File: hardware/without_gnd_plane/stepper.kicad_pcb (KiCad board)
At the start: 4 copper layers, 40 x 40 mm, 132 parts, among them J101 USB-MINI-B-SMD, J102 DRILL, J103 DRILL, J104 DRILL, J105 DRILL, J401 STACK-UP-HIGH, J402 STACK-DOWN, J403 STACK-UP-HIGH, J404 STACK-DOWN, P201 black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

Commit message: version before changing to 6 layers
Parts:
- removed R201: 0, kicad-libraries:0603E
- C105, C106: value 8pF -> 5pF
- RP201: value 100 -> 220
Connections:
- C101 pad 2: GND -> STACK-PGND
- C102 pad 2: GND -> STACK-PGND
- C103 pad 2: GND -> STACK-PGND
- C104 pad 2: GND -> STACK-PGND
- C105 pad 2: GND -> STACK-PGND
- C106 pad 2: GND -> STACK-PGND
- C301 pad 2: GND -> STACK-PGND
- C302 pad 2: GND -> STACK-PGND
- C303 pad 2: GND -> STACK-PGND
- C304 pad 2: GND -> STACK-PGND
- C401 pad 2: GND -> STACK-PGND
- C402 pad 2: GND -> STACK-PGND
- C403 pad 2: GND -> STACK-PGND
- C404 pad 2: GND -> STACK-PGND
- C501 pad 2: GND -> STACK-PGND
- C502 pad 2: GND -> STACK-PGND
- C503 pad 2: GND -> STACK-PGND
- C504 pad 2: GND -> STACK-PGND
- C505 pad 2: GND -> STACK-PGND
- C506 pad 2: GND -> STACK-PGND
- C507 pad 2: GND -> STACK-PGND
- C508 pad 2: GND -> STACK-PGND
- C509 pad 2: GND -> STACK-PGND
- C510 pad 2: GND -> STACK-PGND
- C511 pad 2: GND -> STACK-PGND
- C512 pad 2: GND -> STACK-PGND
- C513 pad 2: GND -> STACK-PGND
- C514 pad 2: GND -> STACK-PGND
- C515 pad 2: GND -> STACK-PGND
- C516 pad 2: GND -> STACK-PGND
- C517 pad 2: GND -> STACK-PGND
- C518 pad 2: GND -> STACK-PGND
- D301 pad 1: GND -> STACK-PGND
- D302 pad 1: GND -> STACK-PGND
- D401 pad 1: GND -> STACK-PGND
- D402 pad 1: GND -> STACK-PGND
- D502 pad 1: GND -> STACK-PGND
- D503 pad 1: GND -> STACK-PGND
- FB102 pad 1: GND -> STACK-PGND
- FILTER301 pad EXP: GND -> STACK-PGND
- FILTER302 pad 14: GND -> STACK-PGND
- FILTER302 pad EXP: GND -> STACK-PGND
- J101 pad 5: GND -> STACK-PGND
- J401 pad EP: GND -> STACK-PGND
- J402 pad EP: GND -> STACK-PGND
- J403 pad 21: GND -> STACK-PGND
- J403 pad 23: GND -> STACK-PGND
- J403 pad 25: GND -> STACK-PGND
- J403 pad 27: GND -> STACK-PGND
- J403 pad EP: GND -> STACK-PGND
- J404 pad 21: GND -> STACK-PGND
- J404 pad 23: GND -> STACK-PGND
- J404 pad 25: GND -> STACK-PGND
- J404 pad 27: GND -> STACK-PGND
- J404 pad EP: GND -> STACK-PGND
- P301 pad 2: GND -> STACK-PGND
- P301 pad EP: GND -> STACK-PGND
- P302 pad 2: GND -> STACK-PGND
- P302 pad EP: GND -> STACK-PGND
- R104 pad 1: GND -> STACK-PGND
- R203 pad 2: GND -> STACK-PGND
- R207 pad 2: GND -> STACK-PGND
- R208 pad 1: GND -> STACK-PGND
- SW101 pad 2: GND -> STACK-PGND
- U101 pad 17: GND -> STACK-PGND
- U101 pad 2: GND -> STACK-PGND
- U101 pad 46: GND -> STACK-PGND
- U101 pad 60: GND -> STACK-PGND
- U102 pad 2: GND -> STACK-PGND
- U501 pad 1: GND -> STACK-PGND
- X101 pad 3: GND -> STACK-PGND
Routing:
- net GND: track 429.1 -> 0.00 mm, vias 65 -> 0
- net STACK-PGND: track 278.6 -> 692.9 mm, vias 70 -> 135
- removed copper zone on B.Cu, net GND
- removed copper zone on GND, net GND
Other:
- board text added: "Silent Stepper 1.0b"
- board text removed: "Silent Stepper 1.0"

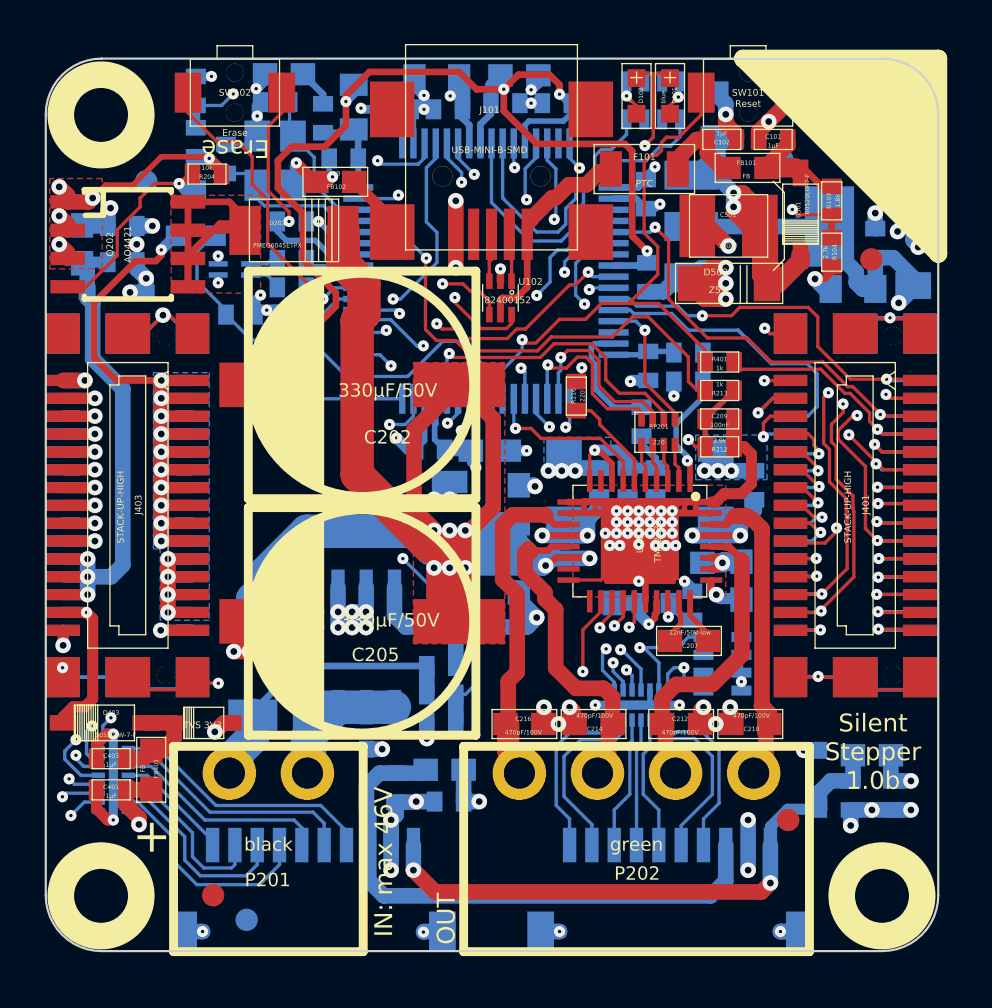
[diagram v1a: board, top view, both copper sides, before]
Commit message: change to 6 layer layout
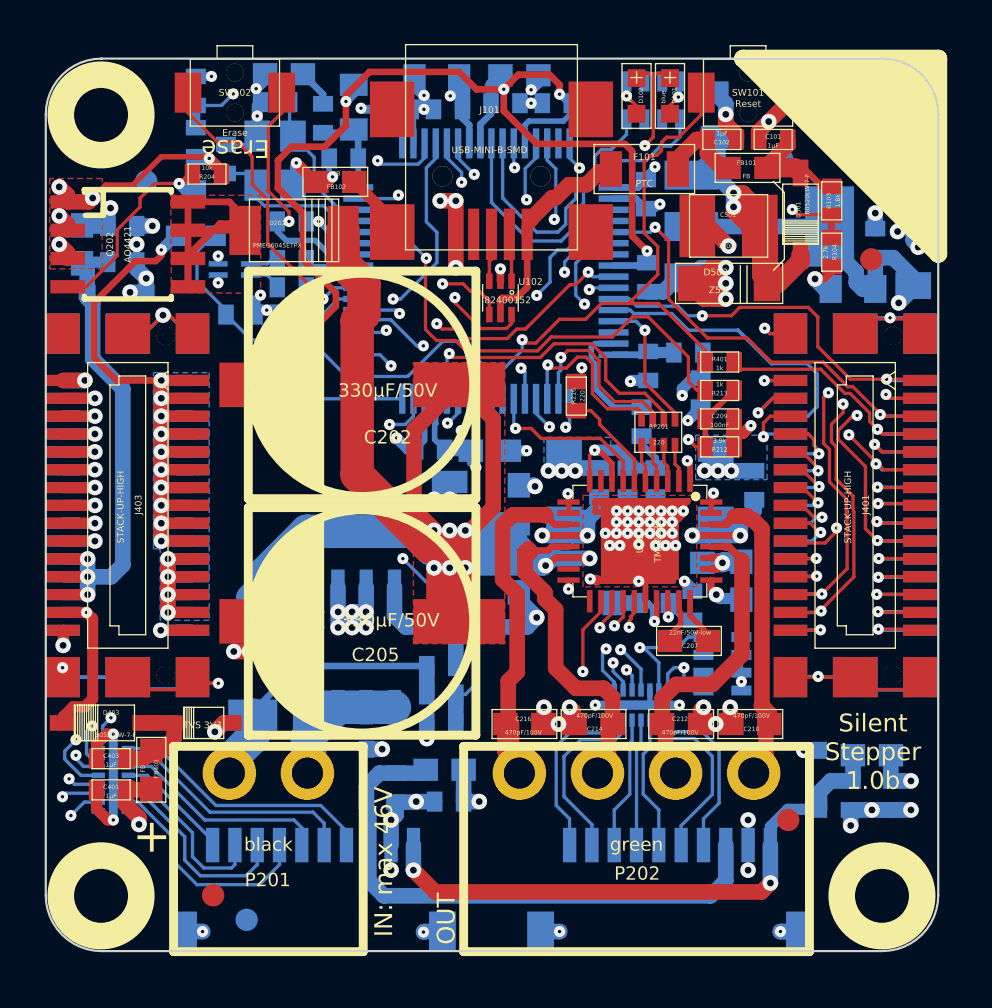
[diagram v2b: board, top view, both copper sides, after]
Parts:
- moved C106 0.74 mm to (156.1, 87.8), turned to 270 degrees
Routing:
- net STACK-PGND: track 692.9 -> 666.4 mm, vias 135 -> 142
- net BRICKLET-IO1_0/AD1: track 47.9 -> 35.4 mm
- net 3V3: track 182.3 -> 176.9 mm
- net BRICKLET-I2C-SCL: track 56.0 -> 58.8 mm
- net Net-(C105-Pad1): track 3.07 -> 4.24 mm
- net STACK-I2C-SCL/JTAG-TDO: track 23.5 -> 24.3 mm
- net STACK-I2C-SDA/JTAG-TDI: track 13.5 -> 14.2 mm
- net STACK-SER-TXD: track 35.8 -> 36.5 mm
- net STACK-SPI-MOSI: track 22.4 -> 23.1 mm
- net STACK-SER-RXD: track 34.7 -> 35.3 mm
- net PWR-CLK: track 6.71 -> 7.00 mm, vias 1 -> 2
- added copper zone on IN4.CU, net STACK-PVCC
- removed copper zone on VCC, net STACK-PVCC
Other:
- copper layers 4 -> 6

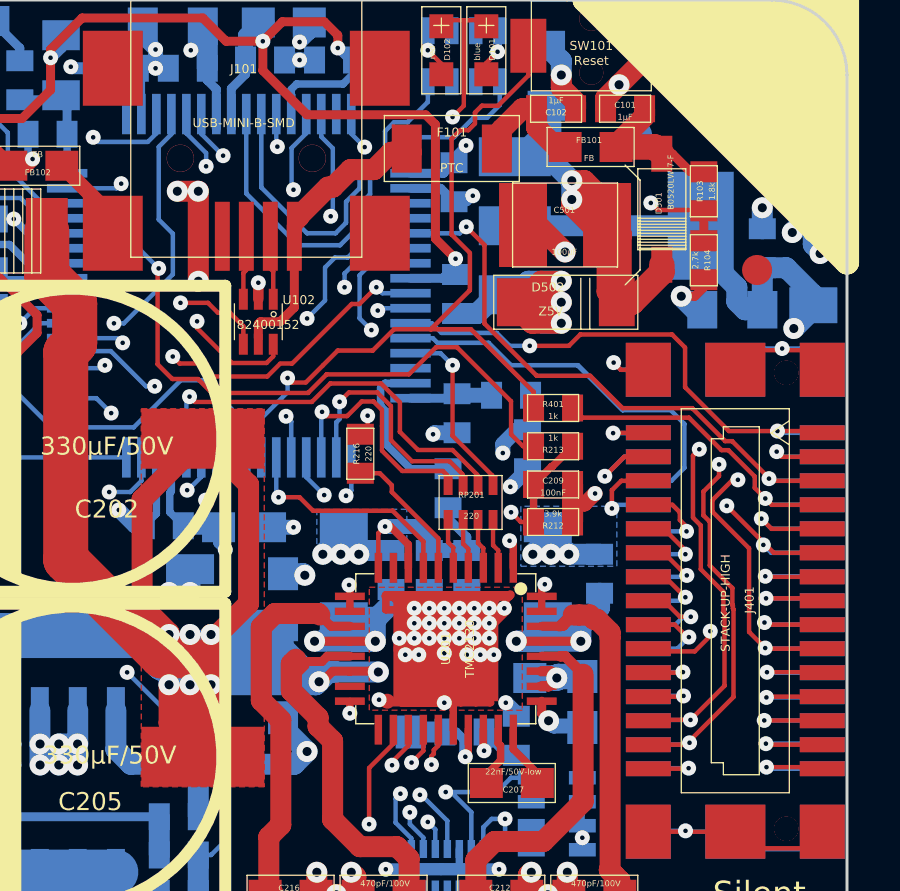
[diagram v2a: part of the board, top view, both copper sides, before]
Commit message: change routing, remove pi filter
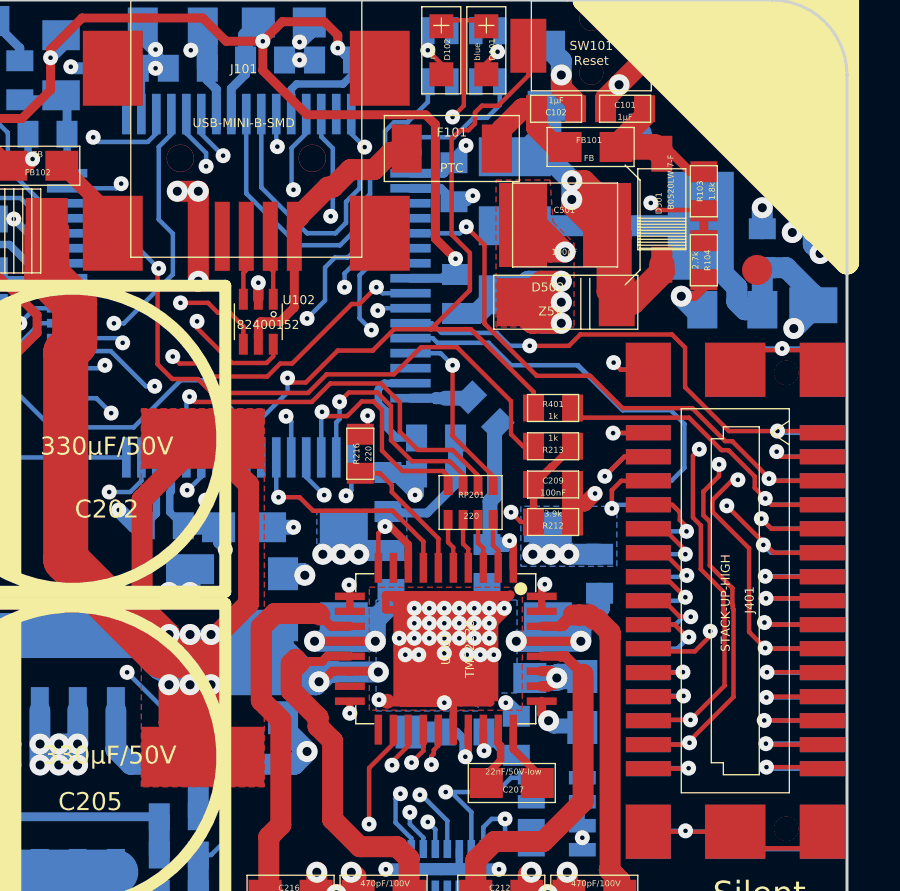
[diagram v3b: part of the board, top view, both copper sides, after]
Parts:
- removed C105, C106: 5pF, kicad-libraries:0402E
- added R201: 1k, kicad-libraries:0402E, B.Cu at (154.7, 91.6)
- R209: value 0 -> FB
- moved R210 3.36 mm to (153.0, 88.6), turned to 180 degrees
- moved C201 2.94 mm to (151.4, 89.2), turned to 270 degrees
- moved R209 1.72 mm to (153.0, 87.4), turned to 0 degrees
- moved R105 1.04 mm to (154.6, 86.5), turned to 315 degrees
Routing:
- net STACK-PGND: track 666.4 -> 669.1 mm, vias 142 -> 141
- net 3V3: track 176.9 -> 178.7 mm
- net Net-(R105-Pad1): track 4.24 -> 3.01 mm
- net PWR-SW-3V3: track 5.42 -> 4.31 mm
- net PWR-CLK: track 7.00 -> 5.89 mm, vias 2 -> 1

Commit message: drc check
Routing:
- net 3V3: track 178.7 -> 169.7 mm
- net PWR-ENABLE: track 20.9 -> 19.6 mm
- net STACK-PGND: track 669.1 -> 669.8 mm, vias 141 -> 142
- net BRICKLET-I2C-SCL: track 58.8 -> 58.1 mm
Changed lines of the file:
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@@
     (links 416)
     (no_connects 2)
-    (area 126.671069 72.726549 166.772591 112.825531)
+    (area 125.845139 71.945139 283.420502 165.440043)
     (thickness 1.6002)
     (drawings 63)
-    (tracks 2691)
+    (tracks 2681)
     (zones 0)
     (modules 130)
@@
     (1 GND signal hide)
     (2 IN2.CU signal hide)
-    (3 IN4.CU signal hide)
+    (3 IN4.CU signal)
     (4 VCC signal hide)
-    (31 Rückseite signal)
+    (31 Rückseite signal hide)
     (32 B.Adhes user)
     (33 F.Adhes user)
@@
   )
   (setup
-    (last_trace_width 0.50038)
+    (last_trace_width 0.1524)
     (user_trace_width 0.1524)
     (user_trace_width 0.25)
@@
     (aux_axis_origin 126.725 72.775)
     (grid_origin 126.725 72.775)
-    (visible_elements FFFFBFFF)
+    (visible_elements FFFF3FFF)
     (pcbplotparams
-      (layerselection 0x010fc_80000007)
+      (layerselection 0x00000_00000008)
       (usegerberextensions true)
       (excludeedgelayer true)
@@
   (segment (start 160.1912 94.487) (end 161.6493 94.487) (width 0.1498) (layer Vorderseite) (net 1))
   (segment (start 160.1019 94.3977) (end 160.1912 94.487) (width 0.1498) (layer Vorderseite) (net 1))
-  (segment (start 160.7222 94.487) (end 161.6493 94.487) (width 0.1498) (layer IN4.CU) (net 1))
-  (segment (start 161.6493 94.487) (end 162.1652 93.9711) (width 0.1498) (layer IN4.CU) (net 1))
-  (segment (start 160.7222 97.8778) (end 157.9 100.7) (width 0.148) (layer IN4.CU) (net 1))
-  (segment (start 160.7222 94.487) (end 160.7222 97.8778) (width 0.1498) (layer IN4.CU) (net 1))
   (via (at 162.1652 93.8151) (size 0.5) (layers Vorderseite Rückseite) (net 1))
   (segment (start 162.1652 93.9711) (end 162.1652 93.8151) (width 0.1498) (layer IN4.CU) (net 1))
@@
   (segment (start 165.6 82.6) (end 165.6 82.9493) (width 0.701) (layer Rückseite) (net 1))
   (segment (start 164.7 81.7) (end 165.6 82.6) (width 0.701) (layer Rückseite) (net 1))
+  (segment (start 155.3247 100.0712) (end 155.3247 100.0753) (width 0.1524) (layer IN4.CU) (net 2))
+  (segment (start 154.2529 101.1471) (end 148.2122 101.1471) (width 0.1524) (layer IN4.CU) (net 2))
+  (segment (start 155.3247 100.0753) (end 154.2529 101.1471) (width 0.1524) (layer IN4.CU) (net 2))
   (segment (start 150.875 89.8) (end 152.8 87.875) (width 0.1524) (layer IN4.CU) (net 2))
   (segment (start 157.825 88.05) (end 157.825 89.9025) (width 0.1524) (layer IN4.CU) (net 2))
@@
   (segment (start 129.275 103.05) (end 129.275 102.6888) (width 0.1498) (layer Rückseite) (net 2))
   (segment (start 129.275 102.6888) (end 129.6435 102.3203) (width 0.1498) (layer Rückseite) (net 2))
-  (segment (start 155.3247 100.0712) (end 154.8772 99.6237) (width 0.1498) (layer IN4.CU) (net 2))
-  (segment (start 154.8772 99.6237) (end 153.8699 99.6237) (width 0.1498) (layer IN4.CU) (net 2))
-  (segment (start 153.8699 99.6237) (end 153.676 99.8176) (width 0.1498) (layer IN4.CU) (net 2))
-  (segment (start 153.676 99.8176) (end 153.676 100.3613) (width 0.1498) (layer IN4.CU) (net 2))
-  (segment (start 153.676 100.3613) (end 152.8902 101.1471) (width 0.1498) (layer IN4.CU) (net 2))
-  (segment (start 152.8902 101.1471) (end 148.2122 101.1471) (width 0.1498) (layer IN4.CU) (net 2))
   (segment (start 148.2122 101.1471) (end 147.0391 102.3202) (width 0.1498) (layer IN4.CU) (net 2))
   (segment (start 147.0391 102.3202) (end 129.6435 102.3202) (width 0.1498) (layer IN4.CU) (net 2))
@@
   (segment (start 147.69968 88.02262) (end 147.69968 89.27468) (width 0.148) (layer Rückseite) (net 13))
   (segment (start 147.69968 89.27468) (end 147.775 89.35) (width 0.148) (layer Rückseite) (net 13))
-  (segment (start 145.9965 88.6535) (end 148 86.65) (width 0.1524) (layer IN4.CU) (net 14))
+  (segment (start 146.4144 95.9356) (end 146.4144 91.7856) (width 0.1524) (layer IN4.CU) (net 14))
+  (segment (start 146.725 87.95) (end 148.025 86.65) (width 0.1524) (layer IN4.CU) (net 14))
+  (segment (start 146.725 91.475) (end 146.725 87.95) (width 0.1524) (layer IN4.CU) (net 14))
+  (segment (start 146.4144 91.7856) (end 146.725 91.475) (width 0.1524) (layer IN4.CU) (net 14))
   (segment (start 148.19752 86.82252) (end 148.025 86.65) (width 0.1524) (layer Rückseite) (net 14))
-  (via (at 148.025 86.65) (size 0.5) (drill 0.15) (layers Vorderseite Rückseite) (net 14))
   (segment (start 148.19752 86.82252) (end 148.19752 88.02262) (width 0.1524) (layer Rückseite) (net 14))
-  (segment (start 148 86.65) (end 148.025 86.65) (width 0.1524) (layer IN4.CU) (net 14))
+  (via (at 148.025 86.65) (size 0.5) (drill 0.15) (layers Vorderseite Rückseite) (net 14))
   (segment (start 151.8204 97.8074) (end 152.2084 98.1954) (width 0.1498) (layer IN4.CU) (net 14))
   (segment (start 151.1827 97.8074) (end 151.8204 97.8074) (width 0.1498) (layer IN4.CU) (net 14))
@@
   (segment (start 148.9632 97.25) (end 149.7593 98.0461) (width 0.1498) (layer IN4.CU) (net 14))
   (segment (start 147.7288 97.25) (end 148.9632 97.25) (width 0.1498) (layer IN4.CU) (net 14))
-  (segment (start 146.3999 95.9211) (end 147.7288 97.25) (width 0.1498) (layer IN4.CU) (net 14))
-  (segment (start 146.3999 93.8433) (end 146.3999 95.9211) (width 0.1498) (layer IN4.CU) (net 14))
-  (segment (start 145.4024 92.8458) (end 146.3999 93.8433) (width 0.1498) (layer IN4.CU) (net 14))
-  (segment (start 145.4024 92.2892) (end 145.4024 92.8458) (width 0.1498) (layer IN4.CU) (net 14))
-  (segment (start 144.9014 91.7882) (end 145.4024 92.2892) (width 0.1498) (layer IN4.CU) (net 14))
-  (segment (start 144.9014 90.5624) (end 144.9014 91.7882) (width 0.1498) (layer IN4.CU) (net 14))
-  (segment (start 145.9965 89.4673) (end 144.9014 90.5624) (width 0.1498) (layer IN4.CU) (net 14))
+  (segment (start 146.4144 95.9356) (end 147.7288 97.25) (width 0.1498) (layer IN4.CU) (net 14))
   (segment (start 152.6007 97.8031) (end 152.2084 98.1954) (width 0.1498) (layer Vorderseite) (net 14))
   (segment (start 152.6007 97.0975) (end 152.6007 97.8031) (width 0.1498) (layer Vorderseite) (net 14))
   (via (at 152.2084 98.1954) (size 0.5) (layers Vorderseite Rückseite) (net 14))
-  (segment (start 145.9965 88.6535) (end 145.9965 89.4673) (width 0.148) (layer IN4.CU) (net 14))
   (segment (start 150.7447 87.0053) (end 150.7447 86.6323) (width 0.1524) (layer Vorderseite) (net 15))
   (via (at 150.7447 86.6323) (size 0.5) (layers Vorderseite Rückseite) (net 15))
@@
   (segment (start 164.0182 94.3977) (end 165.8981 94.3977) (width 0.1498) (layer Rückseite) (net 22))
   (segment (start 163.9963 94.3758) (end 164.0182 94.3977) (width 0.1498) (layer Rückseite) (net 22))
+  (segment (start 144.825 92.525) (end 145.525 92.525) (width 0.70104) (layer Rückseite) (net 23))
+  (via (at 145.525 92.525) (size 0.7) (drill 0.3) (layers Vorderseite Rückseite) (net 23))
   (segment (start 157.325 81.175) (end 156.82452 81.175) (width 0.70104) (layer Vorderseite) (net 23))
   (segment (start 156.82452 81.175) (end 155.92452 80.275) (width 0.70104) (layer Vorderseite) (net 23))
@@
     (polygon
       (pts
-        (xy 149.05 89.75) (xy 149.05 91.45) (xy 152.05 91.45) (xy 152.05 89.75)
+        (xy 149.05 89.75) (xy 149.05 91.6) (xy 152.05 91.6) (xy 152.05 89.75)
       )
     )
@@
       )
     )
+  )
+  (zone (net 23) (net_name STACK-PGND) (layer Rückseite) (hatch edge 0.508)
+    (connect_pads yes (clearance 0.15))
+    (min_thickness 0.3)
+    (fill yes (arc_segments 16) (thermal_gap 0.3) (thermal_bridge_width 0.3))
+    (polygon
+      (pts
+        (xy 138.125 95.675) (xy 138.125 98.725) (xy 141.575 98.725) (xy 141.575 95.675)
+      )
+    )
